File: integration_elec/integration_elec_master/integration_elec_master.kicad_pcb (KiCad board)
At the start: 4 copper layers, 128 x 74.8 mm, 72 parts, among them J1 CONN_02X05, J2 USB_C_Receptacle_USB2.0_16P, Q1 Q_NMOS_GSD, SW1 SW_Push, U1 XBEE_PRO_900HP, U2 STM32F446RETx, U3 USBLC6-2SC6, U4 TPS54335ADDAR, U5 COM-28379, Y1 Crystal_16MHz

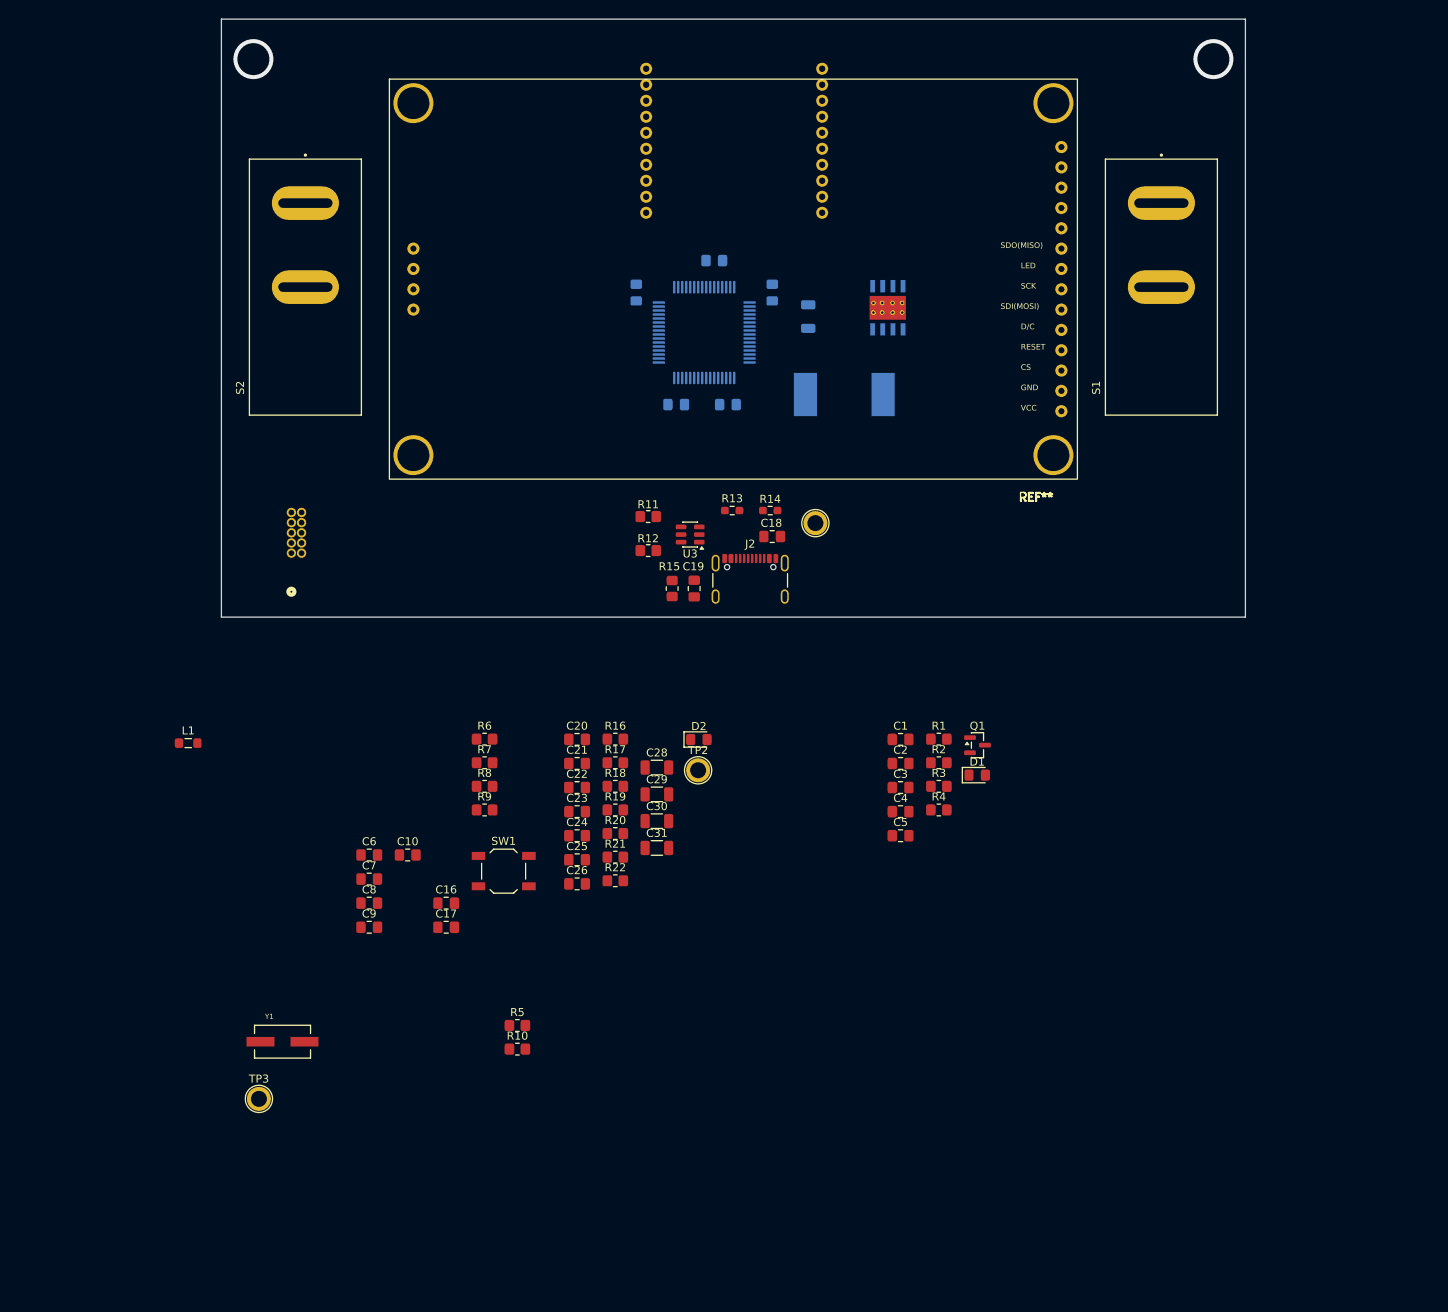
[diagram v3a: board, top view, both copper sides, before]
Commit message: KAH - layout continué, un imbecile a mis le 3v3 tout en bas a droite tres loin de tout
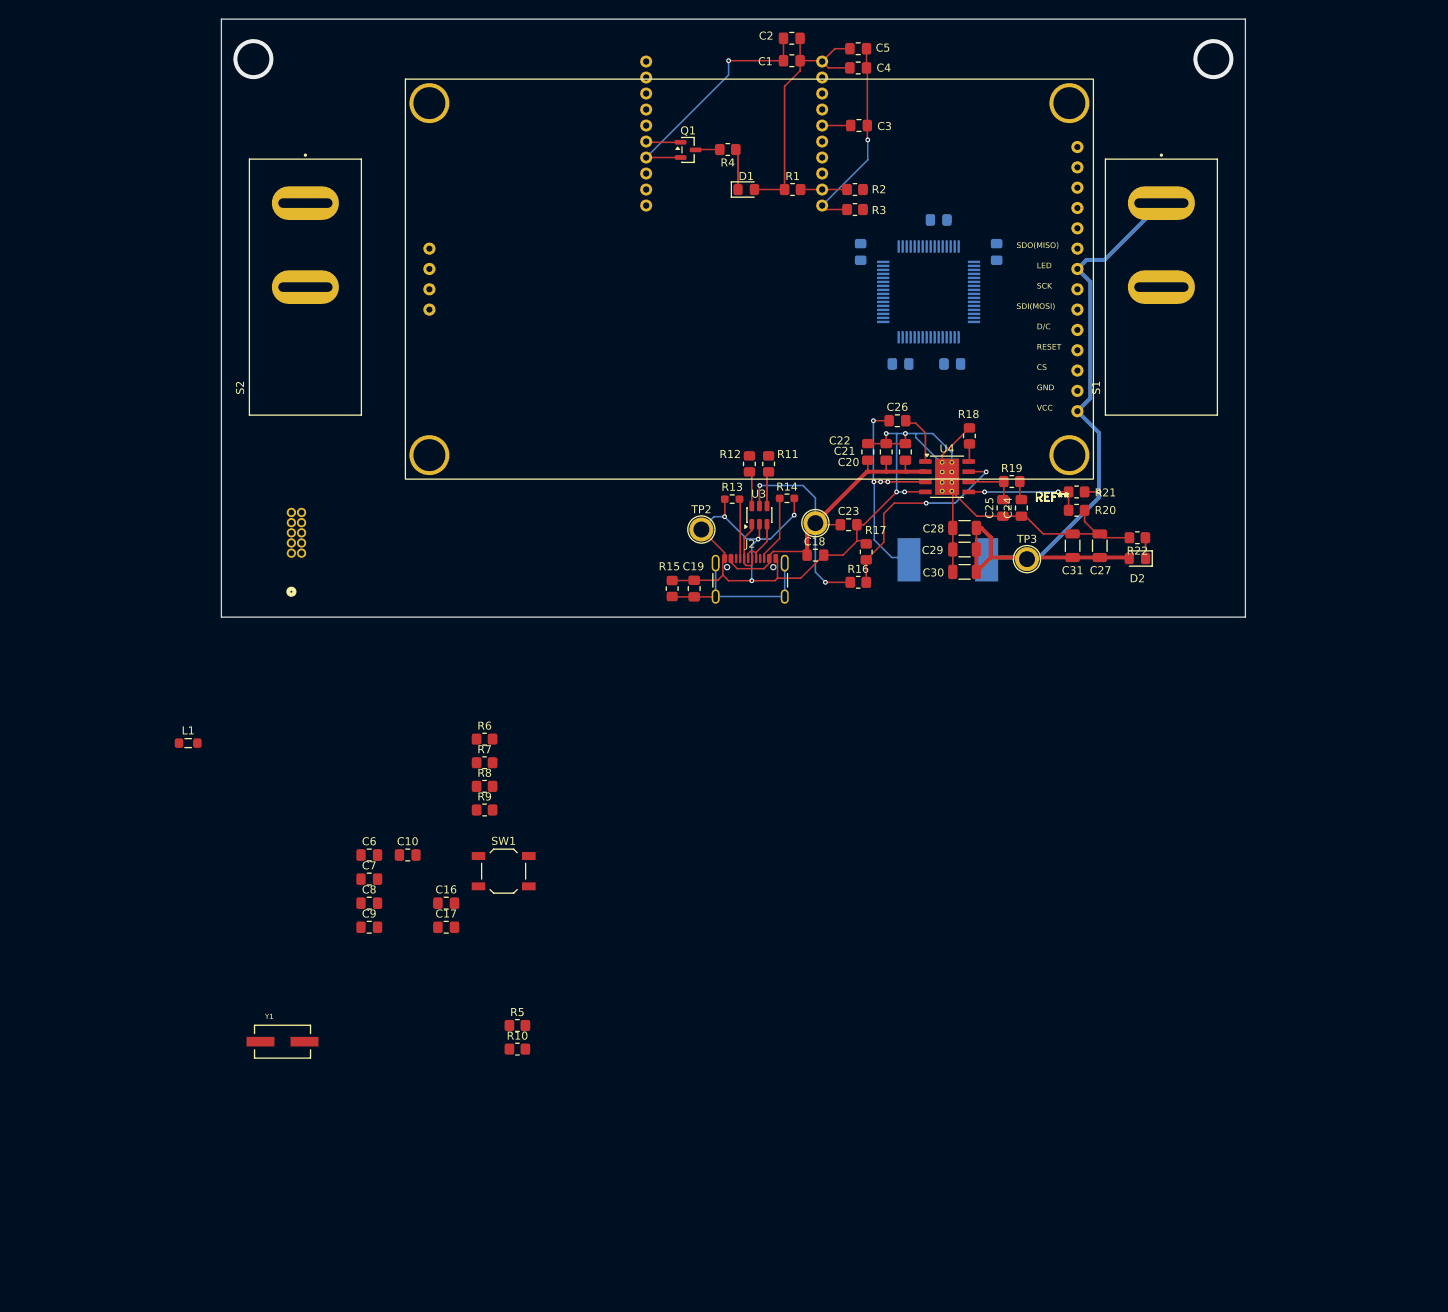
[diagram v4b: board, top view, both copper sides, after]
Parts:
- C27, U4: moved to F.Cu
- moved TP3 117.3 mm to (156.7, 92.5)
- moved C5 98.5 mm to (135.6, 28.7)
- moved C4 93.1 mm to (135.6, 31.1), turned to 180 degrees
- moved C2 91.7 mm to (127.3, 27.4)
- moved R4 86.7 mm to (119.3, 41.3), turned to 180 degrees
- moved C1 85.9 mm to (127.3, 30.2)
- moved C3 82.9 mm to (135.7, 38.3), turned to 180 degrees
- moved Q1 82.7 mm to (114.3, 41.4)
- moved D1 78.7 mm to (121.6, 46.3)
- moved R22 78.1 mm to (170.5, 89.8), turned to 180 degrees
- moved R3 72.9 mm to (135.2, 48.8)
- moved R2 72.4 mm to (135.2, 46.3), turned to 180 degrees
- moved R21 72.1 mm to (162.9, 86.4)
- moved R20 71.8 mm to (162.9, 84.1), turned to 180 degrees
- moved R1 71.1 mm to (127.4, 46.3)
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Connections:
- R9 pad 1: /DEBUG_USB/USB_VBUS -> +5V
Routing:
- net GND: track 0.00 -> 205.9 mm, vias 0 -> 10
- net +3V3: track 0.00 -> 128.3 mm, vias 0 -> 1
- net +5V: track 0.00 -> 64.7 mm, vias 0 -> 2
- net /REGULATOR/PH: track 0.00 -> 29.4 mm, vias 0 -> 4
- net Net-(U4-EN): track 0.00 -> 26.7 mm, vias 0 -> 2
- net Net-(J2-SHIELD): track 0.00 -> 22.5 mm
- net Net-(U4-VSENSE): track 0.00 -> 14.8 mm, vias 0 -> 2
- net Net-(J2-CC2): track 0.00 -> 8.33 mm
- net Net-(J2-CC1): track 0.00 -> 7.46 mm
- net /DEBUG_USB/USB_CONN_D+: track 0.00 -> 7.29 mm
- net /DEBUG_USB/USB_CONN_D-: track 0.00 -> 7.19 mm
- net Net-(U4-COMP): track 0.00 -> 6.72 mm
- net Net-(U4-BOOT): track 0.00 -> 6.60 mm
- net Net-(U1-nDTR): track 0.00 -> 5.80 mm
- net Net-(D1-K): track 0.00 -> 5.11 mm
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
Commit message: KAH - finished layout + routing, waiting for review
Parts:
- C6, C8, L1, R10, R5, R6, R8, SW1, Y1: moved to B.Cu
- moved R5 107.1 mm to (152.2, 61.6), turned to 90 degrees
- moved R10 104.8 mm to (152.3, 67.4), turned to 90 degrees
- moved Y1 94.8 mm to (108.3, 69.2), turned to 90 degrees
- moved C9 93.6 mm to (127.6, 61.4), turned to 180 degrees
- moved C17 84.1 mm to (113.6, 59.8), turned to 90 degrees
- moved L1 81.8 mm to (114.9, 63.4)
- moved C16 81.7 mm to (117.2, 60.8), turned to 180 degrees
- moved C10 80.6 mm to (127.7, 65.0), turned to 180 degrees
- moved C8 78.8 mm to (113.9, 67.3), turned to 90 degrees
- moved C7 77.3 mm to (119.2, 69.4), turned to -90 degrees
- moved R9 75.4 mm to (134.8, 64.0), turned to 180 degrees
- moved C6 70.2 mm to (113.9, 71.4), turned to -90 degrees
- moved SW1 64.7 mm to (100.1, 67.5), turned to 90 degrees
- moved R6 63.7 mm to (117.7, 58.2)
- moved R8 58.1 mm to (126.1, 76.3), turned to 180 degrees
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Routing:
- net +3V3: track 128.3 -> 314.7 mm, vias 1 -> 9
- net GND: track 205.9 -> 339.4 mm, vias 10 -> 19
- net /MCU/VALVE_2: track 0.00 -> 85.8 mm, vias 0 -> 2
- net Net-(R5-Pad2): track 0.00 -> 78.9 mm, vias 0 -> 4
- net /MCU/MISO: track 0.00 -> 56.7 mm, vias 0 -> 1
- net Net-(U2-PA2): track 0.00 -> 52.8 mm, vias 0 -> 4
- net /MCU/D/C: track 0.00 -> 51.3 mm, vias 0 -> 1
- net /MCU/VALVE_1: track 0.00 -> 51.0 mm, vias 0 -> 1
- net /MCU/RF.XBEE_UART_RTS: track 0.00 -> 50.3 mm
- net /MCU/MOSI: track 0.00 -> 50.0 mm, vias 0 -> 1
- net /MCU/CS_TFT: track 0.00 -> 48.9 mm, vias 0 -> 1
- net /MCU/RF.XBEE_LED: track 4.35 -> 53.0 mm, vias 0 -> 1
- net /DEBUG_USB/DEBUG_UART_RX: track 0.00 -> 48.0 mm, vias 0 -> 2
- net /MCU/RF.XBEE_nReset: track 3.57 -> 50.7 mm, vias 0 -> 2
- net /DEBUG_USB/DEBUG_UART_TX: track 0.00 -> 46.8 mm, vias 0 -> 2
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
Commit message: KAH - yipieeee
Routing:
- net GND: track 339.4 -> 347.3 mm, vias 19 -> 20
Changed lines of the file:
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@@
+	)
+	(segment
+		(start 128.7375 65.787557)
+		(end 132.2 69.250057)
+		(width 0.2)
+		(layer "F.Cu")
+		(net 1)
 	)
 	(segment
@@
 	)
 	(segment
+		(start 132.2 69.250057)
+		(end 132.2 69.6)
+		(width 0.2)
+		(layer "F.Cu")
+		(net 1)
+	)
+	(segment
 		(start 135.4375 88.2)
 		(end 136.3 88.2)
@@
 	)
 	(segment
+		(start 128.7375 65)
+		(end 128.7375 65.787557)
+		(width 0.2)
+		(layer "F.Cu")
+		(net 1)
+	)
+	(segment
 		(start 141.405 84.105)
 		(end 144 84.105)
@@
 	)
 	(via
+		(at 132.2 69.6)
+		(size 0.6)
+		(drill 0.3)
+		(layers "F.Cu" "B.Cu")
+		(net 1)
+	)
+	(via
 		(at 141.5 76.8)
 		(size 0.6)
@@
 	)
 	(segment
+		(start 133.5 70.8625)
+		(end 133.4625 70.8625)
+		(width 0.2)
+		(layer "B.Cu")
+		(net 1)
+	)
+	(segment
 		(start 121.049 60.549)
 		(end 120.4 59.9)
@@
 		(width 0.2)
 		(layer "B.Cu")
+		(net 1)
+	)
+	(segment
+		(start 133.4625 70.8625)
+		(end 132.2 69.6)
+		(width 0.2)
+		(layer "B.Cu")

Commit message: EM - Review finale (final i guess)
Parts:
- added H1: MountingHole, MountingHole:MountingHole_3.2mm_M3, F.Cu at (60.4, 29.8)
- added H2: MountingHole, MountingHole:MountingHole_3.2mm_M3, F.Cu at (62.2, 93.9)
- added H3: MountingHole, MountingHole:MountingHole_3.2mm_M3, F.Cu at (178.9, 30.2)
- added H4: MountingHole, MountingHole:MountingHole_3.2mm_M3, F.Cu at (179.0, 94.5)
- moved C6 0.74 mm to (113.9, 70.7)
- moved Y1 0.55 mm to (108.5, 68.7)
- moved C8 0.45 mm to (113.9, 66.9)
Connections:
- R9 pad 1: +5V -> /DEBUG_USB/USB_VBUS
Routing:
- net GND: track 347.3 -> 178.6 mm, vias 20 -> 968
- net +3V3: track 314.7 -> 333.0 mm, vias 9 -> 11
- net +5V: track 84.6 -> 85.3 mm
- net /MCU/VALVE_2: vias 2 -> 1
- net (no net): vias 2 -> 0
- added copper zone on B.Cu, net GND
- added copper zone on F.Cu, net GND
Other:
- copper layers 4 -> 2
